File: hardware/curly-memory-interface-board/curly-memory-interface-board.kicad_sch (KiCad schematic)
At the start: 27 parts, among them J101 Conn_01x05, J102 Conn_01x05, J107 AudioJack2

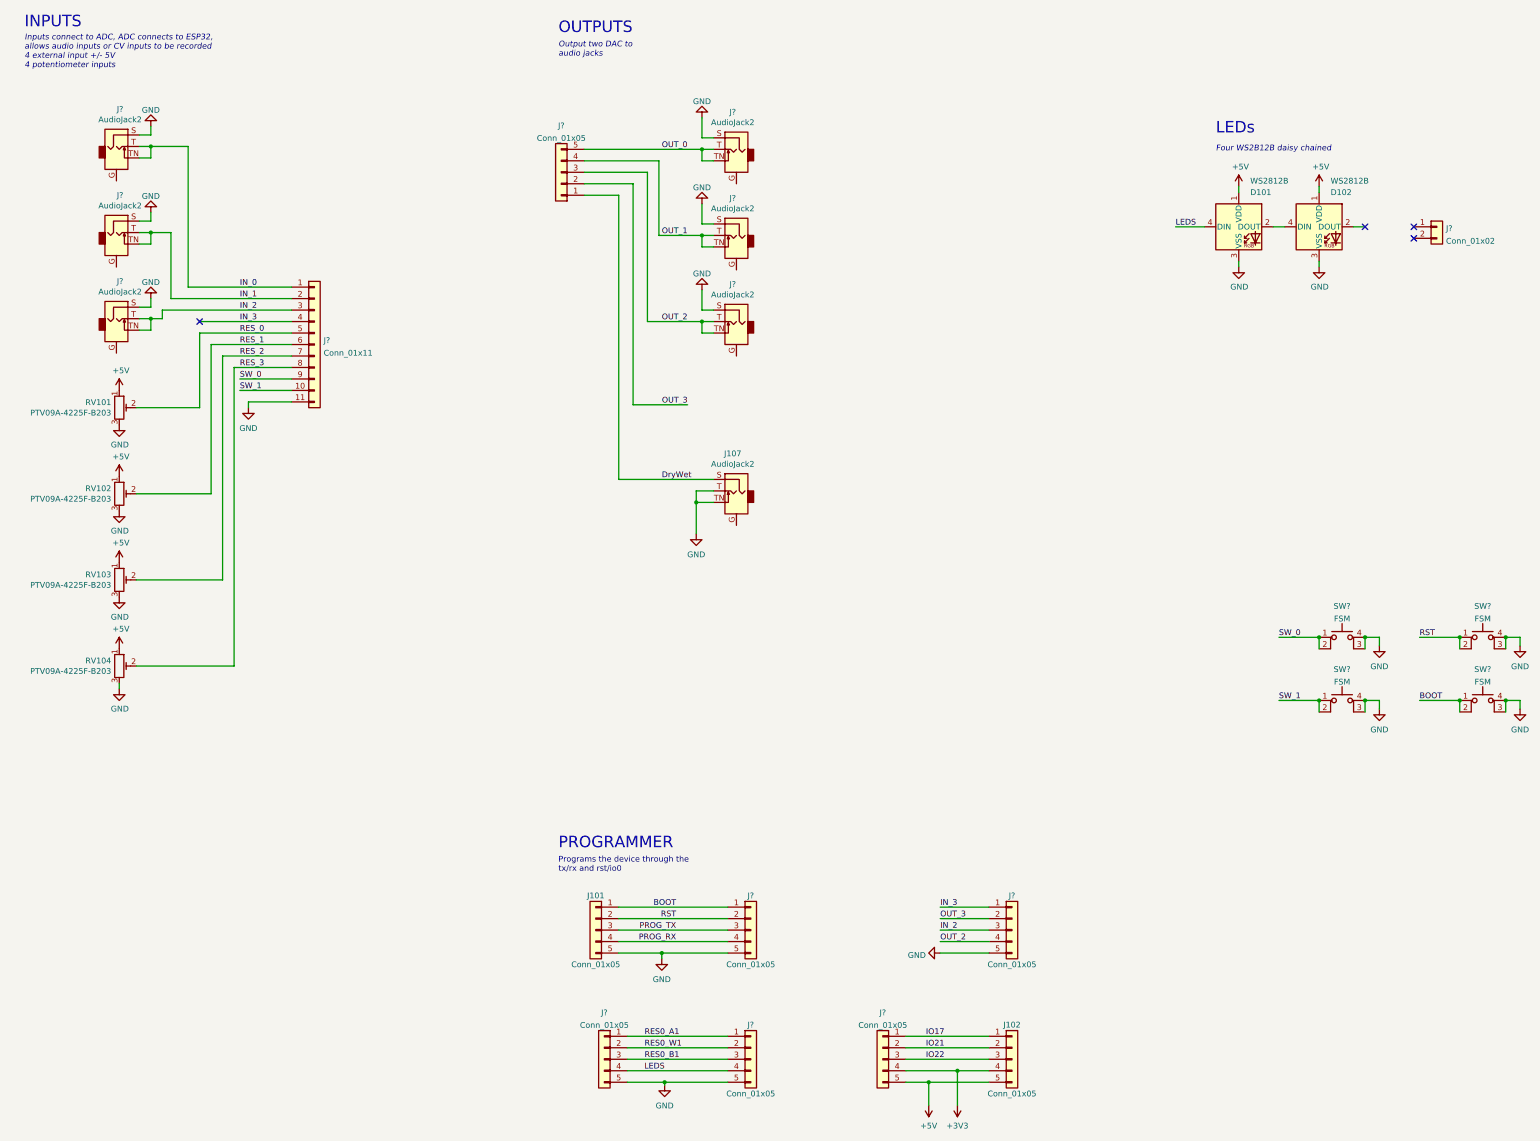
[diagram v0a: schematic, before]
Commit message: all components placed on the main board
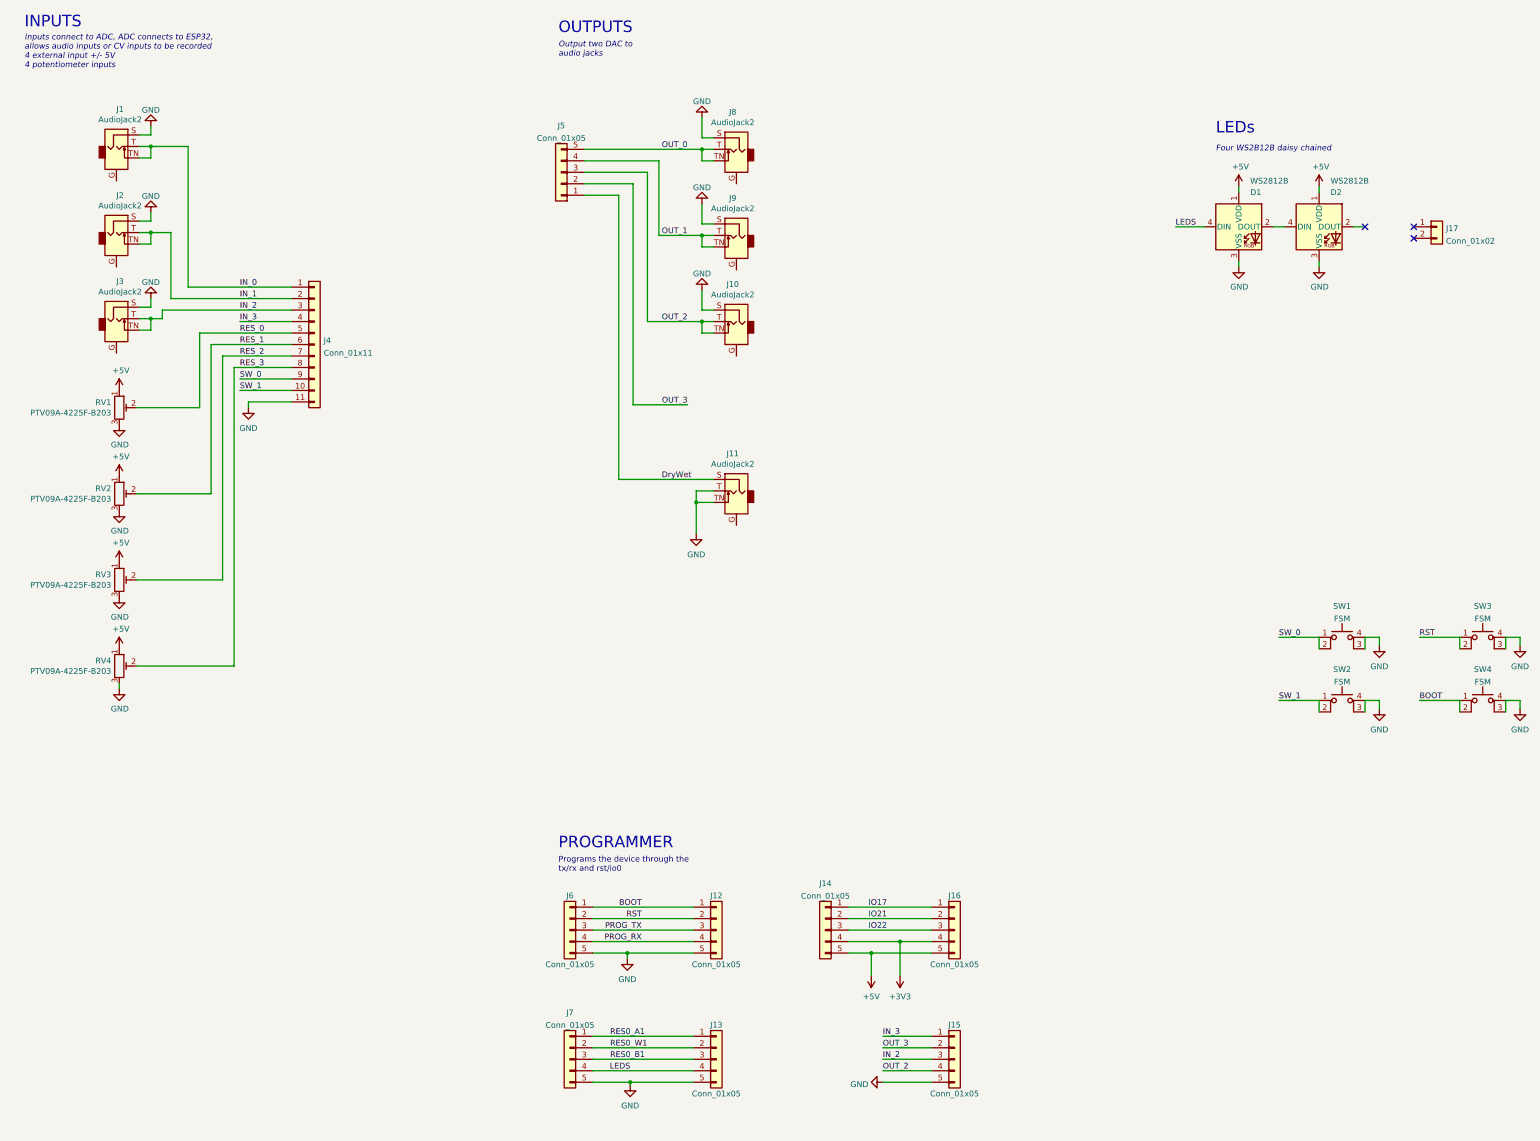
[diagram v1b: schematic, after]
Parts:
- J14: renamed from J?; footprint (none) -> Connector_PinSocket_2.54mm:PinSocket_1x05_P2.54mm_Vertical
- J16: renamed from J102; footprint Connector_PinSocket_2.54mm:PinSocket_1x05_P2.54mm_Vertical -> Connector_PinHeader_2.54mm:PinHeader_1x05_P2.54mm_Vertical
- gave numbers to parts that had none: 17
- renumbered D101 to D1, D102 to D2, J107 to J11, J101 to J6, RV101 to RV1, RV102 to RV2, RV103 to RV3, RV104 to RV4
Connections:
- no-connect marks 4 -> 3
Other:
- moved on the sheet: J12, J13, J14, J15, J16, J6, J7

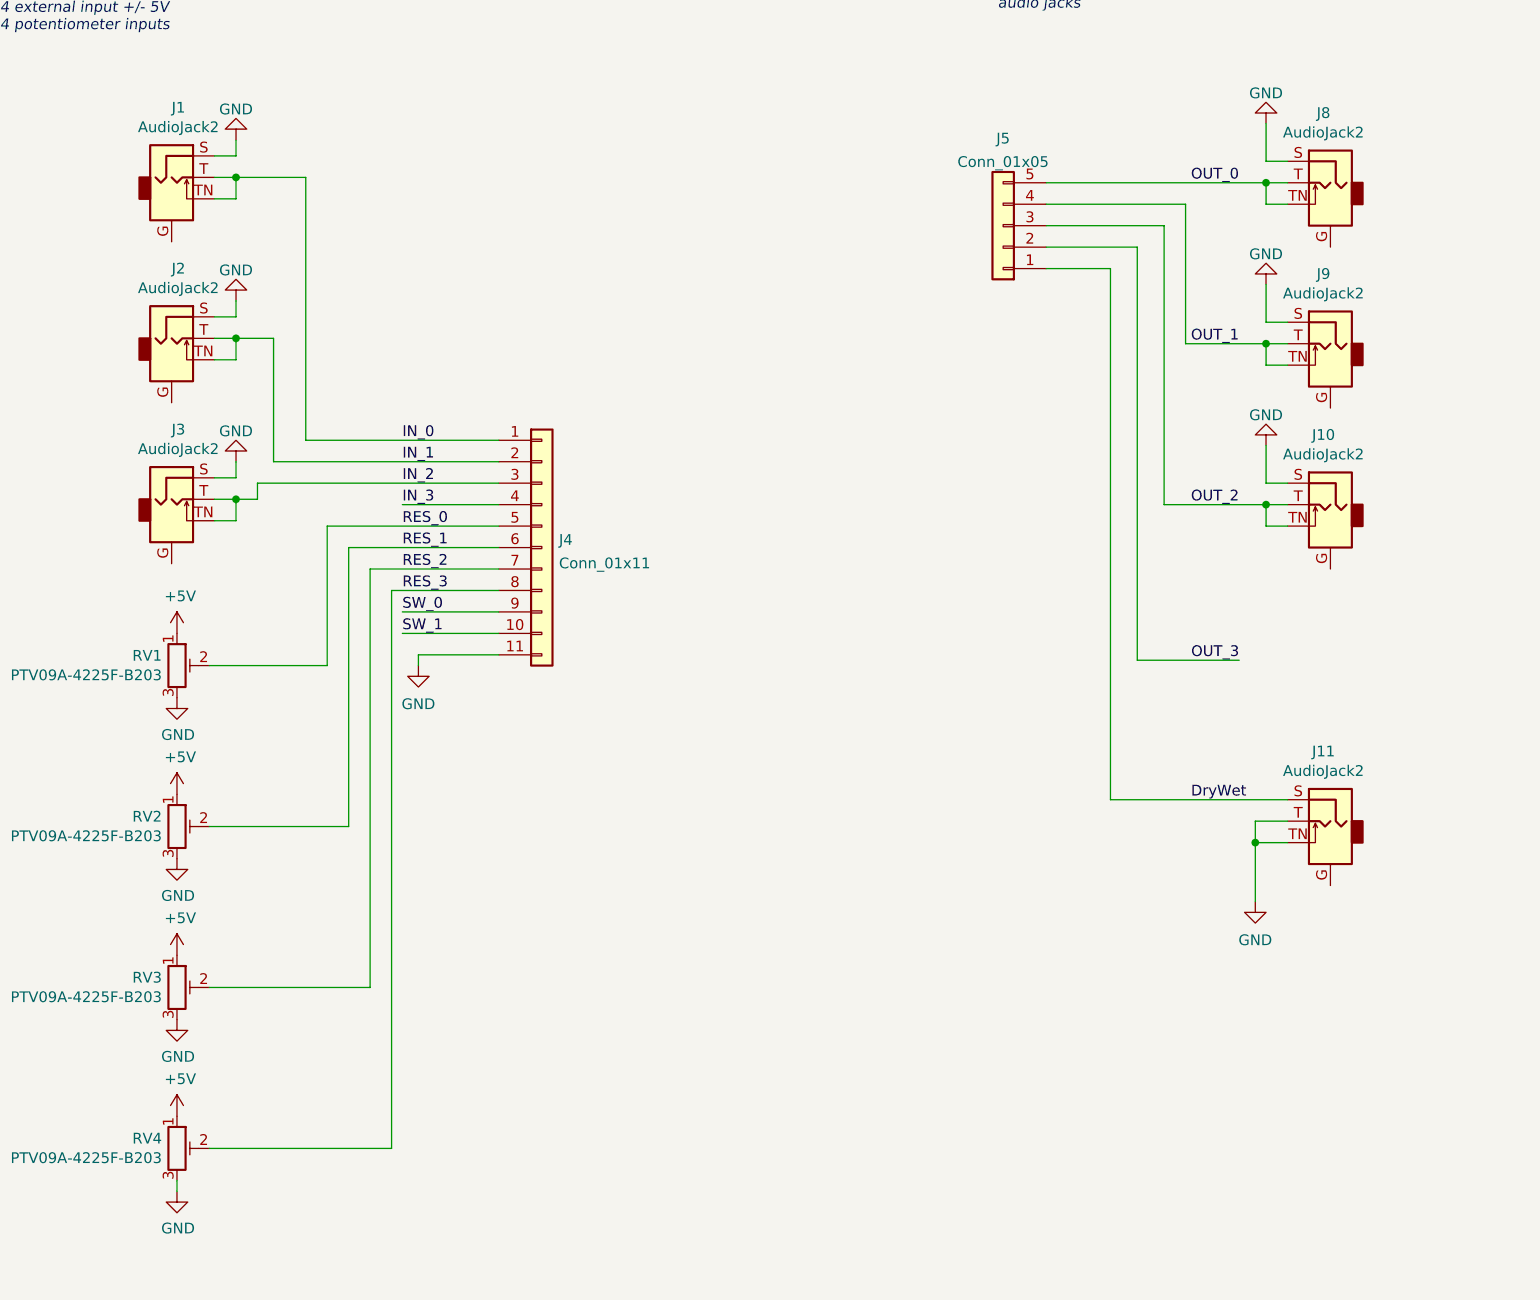
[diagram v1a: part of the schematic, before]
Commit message: more pcb tracked
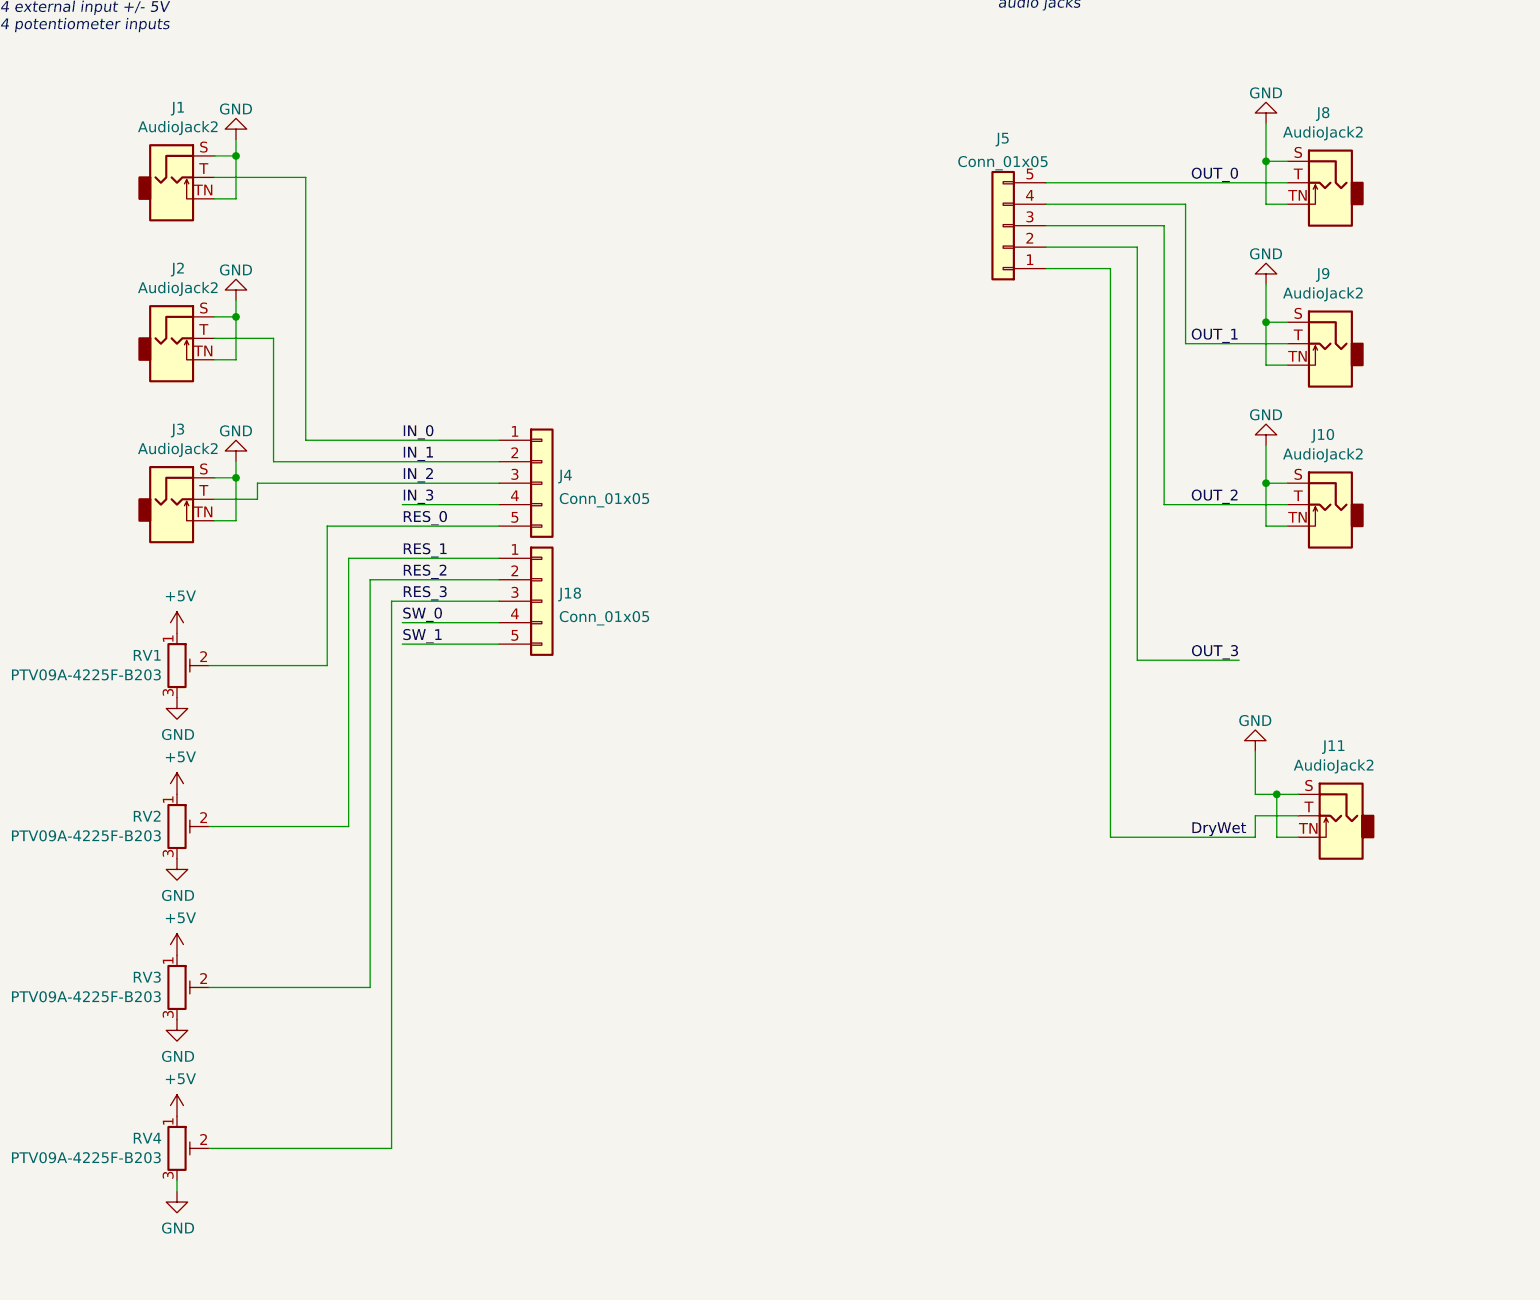
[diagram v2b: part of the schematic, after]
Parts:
- added J18: Conn_01x05, Connector_PinSocket_2.54mm:PinSocket_1x05_P2.54mm_Vertical, symbol Connector_Generic:Conn_01x05
- J1, J10, J11, J2, J3, J8, J9: symbol Connector:AudioJack2_Ground_SwitchT -> Connector:AudioJack2_SwitchT
- J4: value Conn_01x11 -> Conn_01x05; footprint Connector_PinSocket_2.54mm:PinSocket_1x11_P2.54mm_Vertical -> Connector_PinSocket_2.54mm:PinSocket_1x05_P2.54mm_Vertical; symbol Connector_Generic:Conn_01x11 -> Connector_Generic:Conn_01x05
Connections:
- net DryWet: now also J11.T; no longer J11.S
- net GND: now also J1.TN, J10.TN, J11.S, J2.TN, J3.TN, J8.TN, J9.TN; no longer J11.T, J4.11 (Pin_11)
- net IN_0: no longer J1.TN
- net IN_1: no longer J2.TN
- net IN_2: no longer J3.TN
- net OUT_0: no longer J8.TN
- net OUT_1: no longer J9.TN
- net OUT_2: no longer J10.TN
- net RES_1: now also J18.1 (Pin_1); no longer J4.6 (Pin_6)
- net RES_2: now also J18.2 (Pin_2); no longer J4.7 (Pin_7)
- net RES_3: now also J18.3 (Pin_3); no longer J4.8 (Pin_8)
- net SW_0: now also J18.4 (Pin_4); no longer J4.9 (Pin_9)
- net SW_1: now also J18.5 (Pin_5); no longer J4.10 (Pin_10)
